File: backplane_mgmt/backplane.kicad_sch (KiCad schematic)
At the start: 16 parts, among them J201 Backplane, SW201 Blue, U201 74HC2G17, U202 74LVC1G07, U203 AT24CS32-SSHM

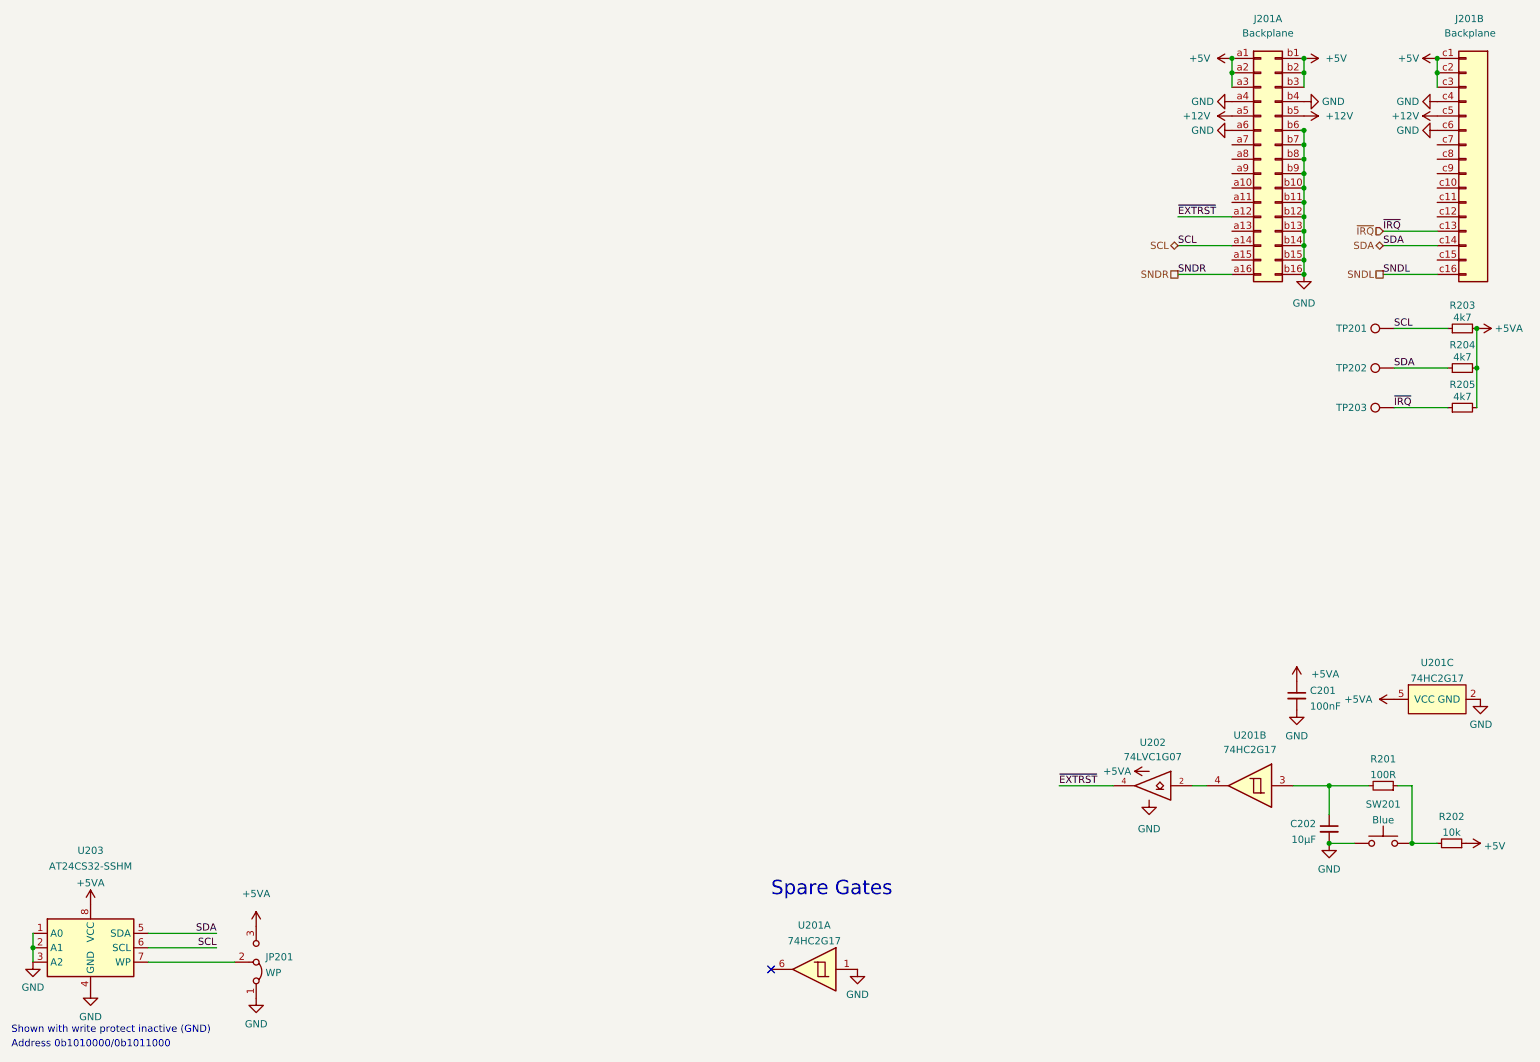
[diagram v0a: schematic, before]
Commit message: Routed backplane mgmt board
- Finished routing of the complete backplane management board; it
  doesn't do much other than provide power (with monitoring) and an
  audio output (with volume control) from the backplane.

  Originally this was gonna have a display but there's no space on the
  front panel for that.
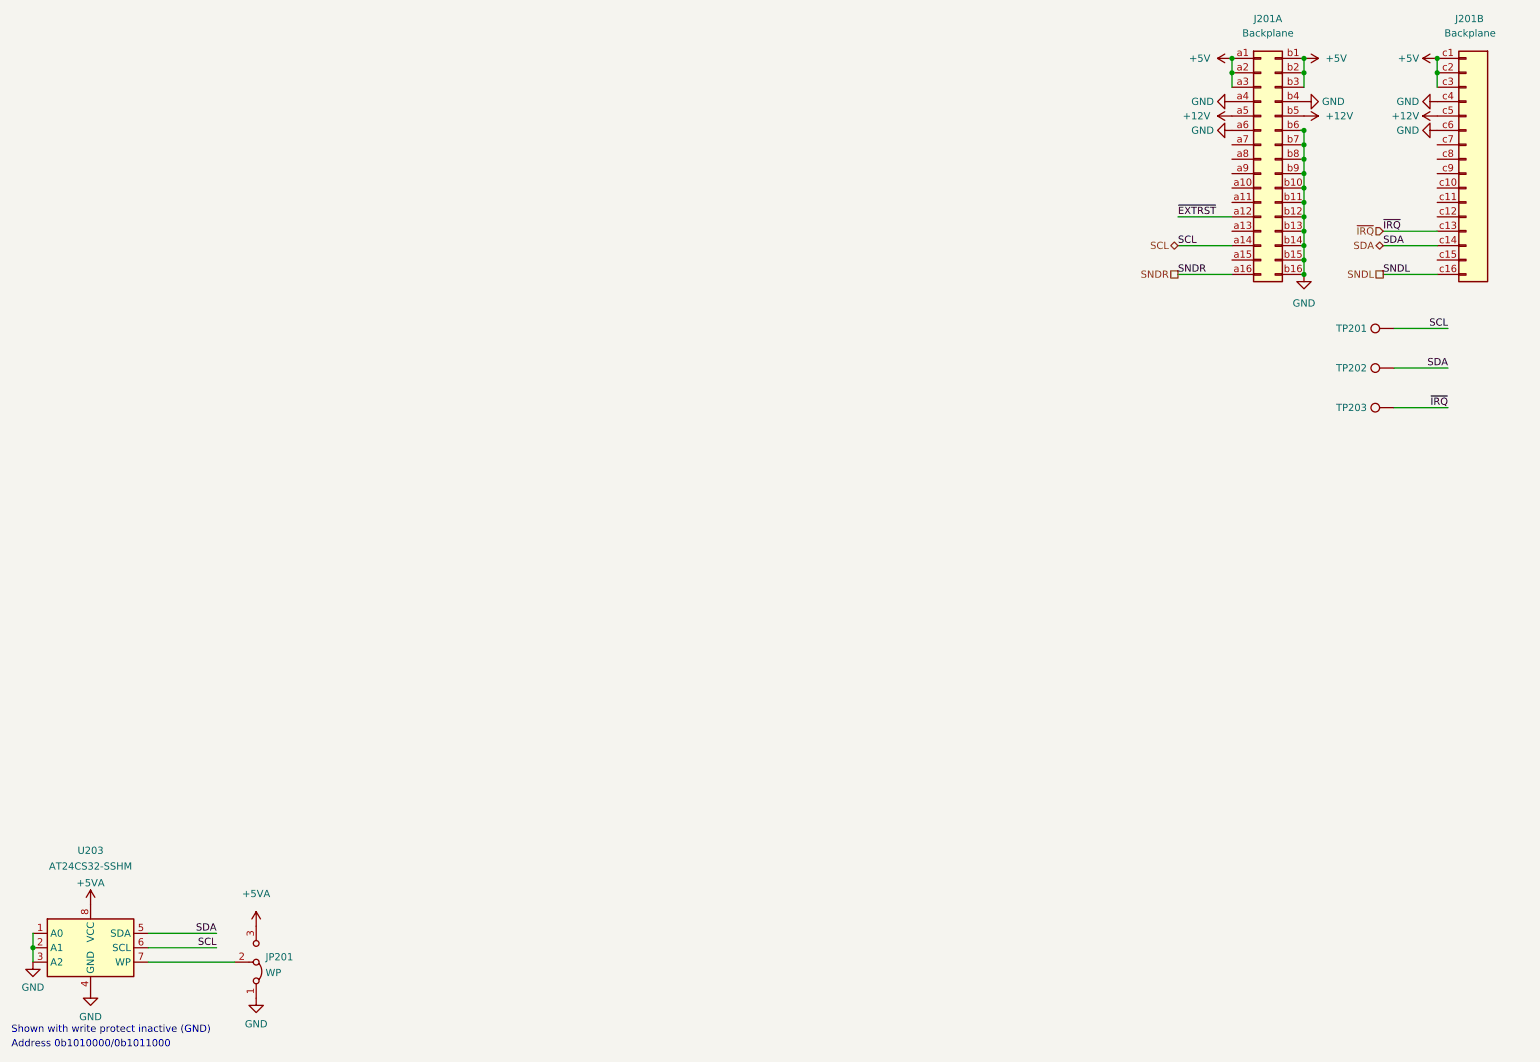
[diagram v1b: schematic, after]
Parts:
- removed C201: 100nF, Capacitor_SMD:C_0805_2012Metric, symbol Device:C_Small
- removed C202: 10µF, Capacitor_SMD:C_0805_2012Metric, symbol Device:C_Small
- removed R201: 100R, Resistor_SMD:R_0805_2012Metric, symbol Device:R_Small
- removed R202: 10k, Resistor_SMD:R_0805_2012Metric, symbol Device:R_Small
- removed R203, R204, R205: 4k7, Resistor_SMD:R_0805_2012Metric, symbol Device:R_Small
- removed SW201: Blue, Button_Switch_THT:SW_Tactile_SPST_Angled_PTS645Vx83-2LFS, symbol Switch:SW_Push
- removed U201: 74HC2G17, Package_SO:TSOP-6_1.65x3.05mm_P0.95mm, symbol 68komputer-common:74HC2G17
- removed U202: 74LVC1G07, 68komputer-common:SC-74-5_1.5x2.9mm_P0.95mm, symbol 74xGxx:74LVC1G07
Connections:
- no-connect marks 1 -> 0
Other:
- note removed: "Spare Gates"

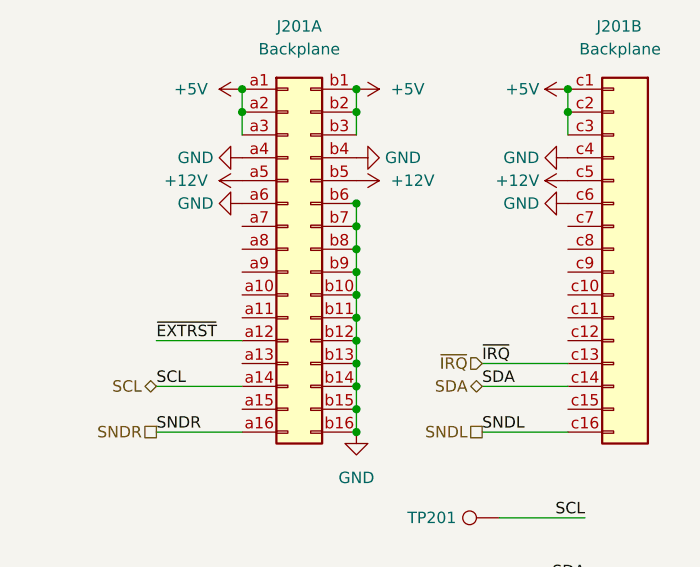
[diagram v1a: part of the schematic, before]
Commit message: Minor tweaks to all boards
- Moved around some traces on the 68000 CPU card for prettiness

- Added a connector on the backplane to provide +5V/+12V without a
  management card installed (for testing)
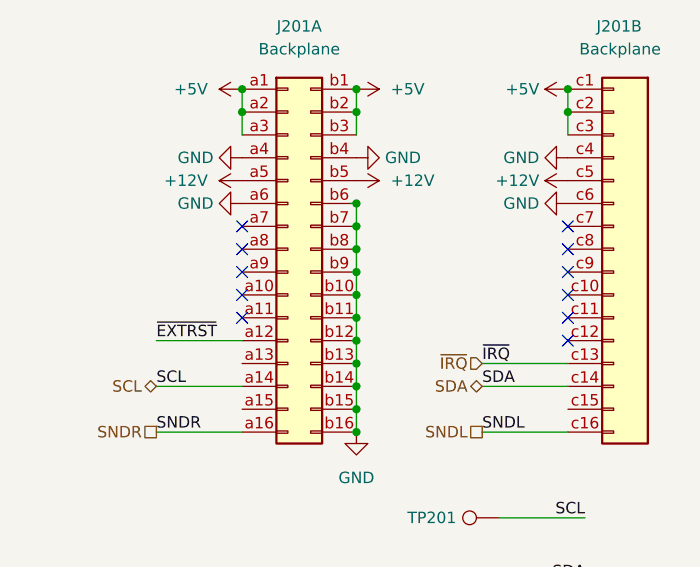
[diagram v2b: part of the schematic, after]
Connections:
- no-connect marks 0 -> 11
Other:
- company: (none) -> Tristan Seifert
- title: (none) -> Backplane Management and Power
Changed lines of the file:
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@@
 (kicad_sch (version 20211123) (generator eeschema)
   (paper "A4")
+  (title_block
+    (title "Backplane Management and Power")
+    (date "2022-01-09")
+    (rev "1")
+    (company "Tristan Seifert")
+  )
   (junction (at 245.11 24.13) (diameter 0) (color 0 0 0 0)
   )
@@
   (junction (at 20.955 178.435) (diameter 0) (color 0 0 0 0)
   )
+  (no_connect (at 232.41 46.99))
+  (no_connect (at 268.605 36.83))
+  (no_connect (at 232.41 44.45))
+  (no_connect (at 268.605 44.45))
+  (no_connect (at 268.605 41.91))
+  (no_connect (at 268.605 46.99))
+  (no_connect (at 232.41 41.91))
+  (no_connect (at 268.605 49.53))
+  (no_connect (at 232.41 39.37))
+  (no_connect (at 232.41 36.83))
+  (no_connect (at 268.605 39.37))
   (wire (pts (xy 245.11 59.69) (xy 245.11 57.15))
     (stroke (width 0) (type default) (color 0 0 0 0))

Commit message: Tweaks to bill of materials
- Added missing MPN's for a few components; tweaked a few bits of layout
  to increase some tolerances

  This includes kind of tweaking the boot rom socket positions in hopes
  of fitting fancier sockets
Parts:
- JP201: now left out of the parts list
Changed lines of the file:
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@@
   )
   (symbol (lib_id "Jumper:Jumper_3_Bridged12") (at 60.325 180.975 270) (mirror x) (unit 1)
-    (in_bom yes) (on_board yes) (fields_autoplaced)
+    (in_bom no) (on_board yes) (fields_autoplaced)
     (property "Reference" "JP201" (id 0) (at 61.976 180.0665 90)
       (effects (font (size 1.27 1.27)) (justify left))

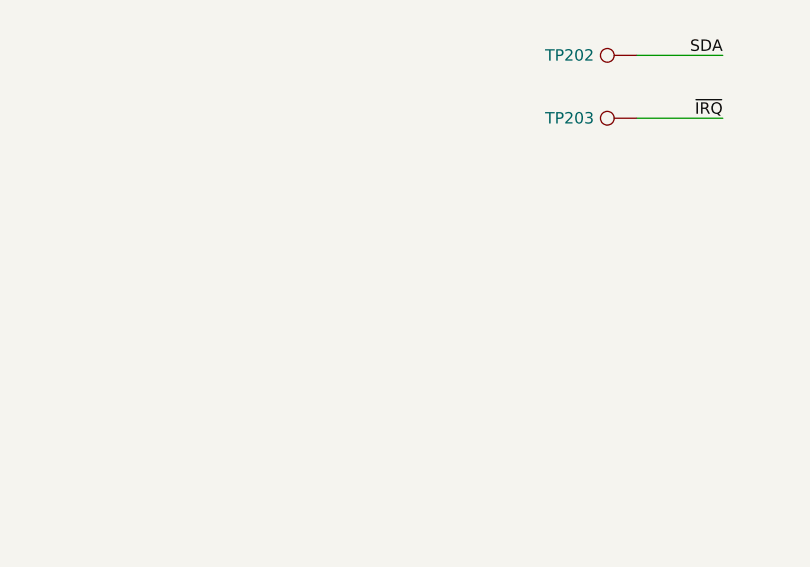
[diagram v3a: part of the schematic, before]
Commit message: Tweaks to backplane management board
- Added pull downs to the audio inputs, so that if the backplane doesn't
  provide audio, the op amp inputs aren't floating

- Minor tweaks to some of the routing. Also switched out the 5V
  regulator for a larger, easier to get version, and added some large
  planes for power dissapation.
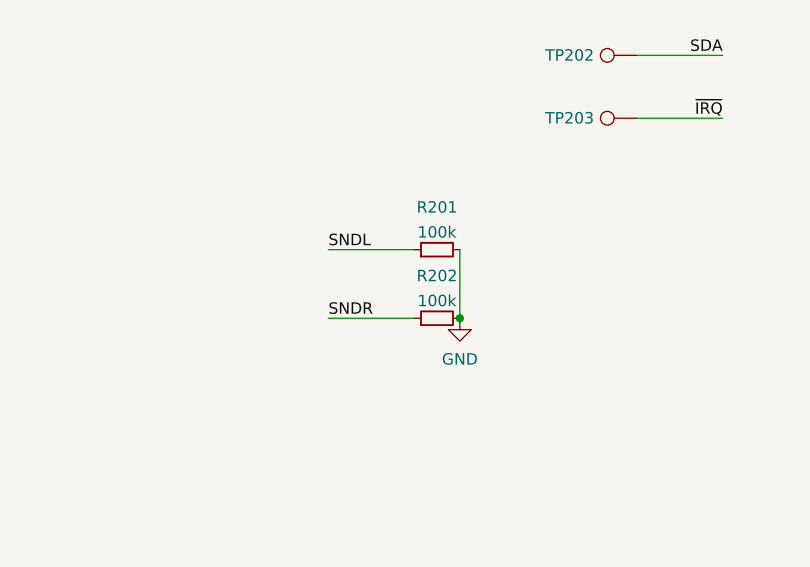
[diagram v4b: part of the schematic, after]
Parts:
- added R201, R202: 100k, Resistor_SMD:R_0805_2012Metric, symbol Device:R_Small
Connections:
- net GND: now also R201.2, R202.2
- net SNDL: now also R201.1
- net SNDR: now also R202.1
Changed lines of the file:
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@@
     (company "Tristan Seifert")
+  )
+  (junction (at 241.3 105.41) (diameter 0) (color 0 0 0 0)
   )
   (junction (at 245.11 24.13) (diameter 0) (color 0 0 0 0)
@@
     (stroke (width 0) (type default) (color 0 0 0 0))
   )
+  (wire (pts (xy 226.695 97.79) (xy 236.22 97.79))
+    (stroke (width 0) (type default) (color 0 0 0 0))
+  )
   (wire (pts (xy 41.275 180.975) (xy 56.515 180.975))
+    (stroke (width 0) (type default) (color 0 0 0 0))
+  )
+  (wire (pts (xy 226.695 105.41) (xy 236.22 105.41))
+    (stroke (width 0) (type default) (color 0 0 0 0))
+  )
+  (wire (pts (xy 241.3 97.79) (xy 241.3 105.41))
     (stroke (width 0) (type default) (color 0 0 0 0))
   )
@@
     (effects (font (size 1.27 1.27)) (justify left bottom))
   )
+  (label "SNDL" (at 226.695 97.79 0)
+    (effects (font (size 1.27 1.27)) (justify left bottom))
+  )
   (label "SDA" (at 270.51 76.2 180)
     (effects (font (size 1.27 1.27)) (justify right bottom))
   )
+  (label "SNDR" (at 226.695 105.41 0)
+    (effects (font (size 1.27 1.27)) (justify left bottom))
+  )
   (label "SNDR" (at 222.885 59.69 0)
     (effects (font (size 1.27 1.27)) (justify left bottom))
@@
     )
     (property "Datasheet" "" (id 3) (at 245.11 21.59 0)
+      (effects (font (size 1.27 1.27)) hide)
+    )
+    (pin "1")
+  )
+  (symbol (lib_id "power:GND") (at 241.3 105.41 0) (unit 1)
+    (in_bom yes) (on_board yes) (fields_autoplaced)
+    (property "Reference" "#PWR0110" (id 0) (at 241.3 111.76 0)
+      (effects (font (size 1.27 1.27)) hide)
+    )
+    (property "Value" "GND" (id 1) (at 241.3 109.9725 0))
+    (property "Footprint" "" (id 2) (at 241.3 105.41 0)
+      (effects (font (size 1.27 1.27)) hide)
+    )
+    (property "Datasheet" "" (id 3) (at 241.3 105.41 0)
       (effects (font (size 1.27 1.27)) hide)
     )
@@
     (pin "8")
   )
+  (symbol (lib_id "Device:R_Small") (at 238.76 105.41 90) (unit 1)
+    (in_bom yes) (on_board yes) (fields_autoplaced)
+    (property "Reference" "R202" (id 0) (at 238.76 100.7069 90))
+    (property "Value" "100k" (id 1) (at 238.76 103.482 90))
+    (property "Footprint" "Resistor_SMD:R_0805_2012Metric" (id 2) (at 238.76 105.41 0)
+      (effects (font (size 1.27 1.27)) hide)
+    )
+    (property "Datasheet" "~" (id 3) (at 238.76 105.41 0)
+      (effects (font (size 1.27 1.27)) hide)
+    )
+    (pin "1")
+    (pin "2")
+  )
   (symbol (lib_id "power:GND") (at 268.605 34.29 270) (unit 1)
     (in_bom yes) (on_board yes) (fields_autoplaced)
@@
     (pin "3")
   )
+  (symbol (lib_id "Device:R_Small") (at 238.76 97.79 90) (unit 1)
+    (in_bom yes) (on_board yes) (fields_autoplaced)
+    (property "Reference" "R201" (id 0) (at 238.76 93.0869 90))
+    (property "Value" "100k" (id 1) (at 238.76 95.862 90))
+    (property "Footprint" "Resistor_SMD:R_0805_2012Metric" (id 2) (at 238.76 97.79 0)
+      (effects (font (size 1.27 1.27)) hide)
+    )
+    (property "Datasheet" "~" (id 3) (at 238.76 97.79 0)
+      (effects (font (size 1.27 1.27)) hide)
+    )
+    (pin "1")
+    (pin "2")
+  )
   (symbol (lib_id "power:GND") (at 31.115 186.055 0) (unit 1)

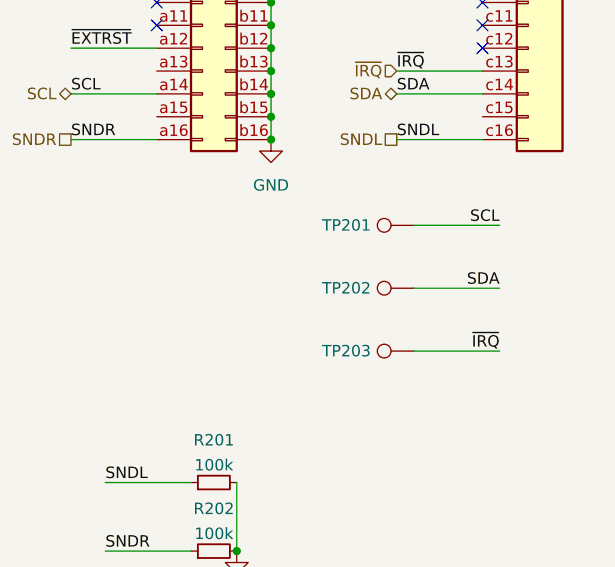
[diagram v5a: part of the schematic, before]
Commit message: Replaced current sense with shunt+INA209
- Instead of using unobtanium parts for the current sensing, we're
  instead just gonna use more of the shunt we already have to get for
  the current limit of the switching regulator, and then measuring the
  voltage drop with the INA209 which is functionally going to give us
  the same exact behavior as before.
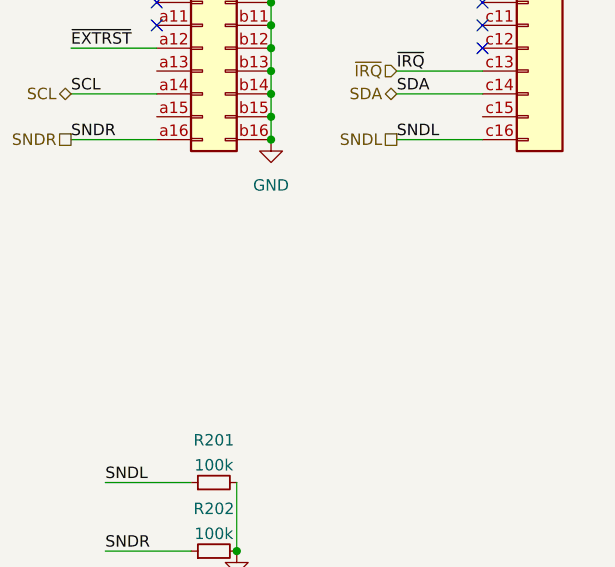
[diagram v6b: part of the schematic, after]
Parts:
- removed TP201: SCL, TestPoint:TestPoint_Loop_D2.60mm_Drill1.4mm_Beaded, symbol Connector:TestPoint
- removed TP202: SDA, TestPoint:TestPoint_Loop_D2.60mm_Drill1.4mm_Beaded, symbol Connector:TestPoint
- removed TP203: ~{IRQ}, TestPoint:TestPoint_Loop_D2.60mm_Drill1.4mm_Beaded, symbol Connector:TestPoint
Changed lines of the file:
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@@
-    (stroke (width 0) (type default) (color 0 0 0 0))
-  )
-  (wire (pts (xy 260.985 69.215) (xy 270.51 69.215))
     (stroke (width 0) (type default) (color 0 0 0 0))
   )
@@
     (stroke (width 0) (type default) (color 0 0 0 0))
   )
-  (wire (pts (xy 260.985 83.185) (xy 270.51 83.185))
-    (stroke (width 0) (type default) (color 0 0 0 0))
-  )
   (wire (pts (xy 245.11 49.53) (xy 245.11 46.99))
     (stroke (width 0) (type default) (color 0 0 0 0))
@@
     (stroke (width 0) (type default) (color 0 0 0 0))
   )
-  (wire (pts (xy 260.985 76.2) (xy 270.51 76.2))
-    (stroke (width 0) (type default) (color 0 0 0 0))
-  )
   (wire (pts (xy 245.11 44.45) (xy 245.11 41.91))
     (stroke (width 0) (type default) (color 0 0 0 0))
@@
     (effects (font (size 1.27 1.27)) (justify left bottom))
   )
-  (label "~{IRQ}" (at 270.51 83.185 180)
-    (effects (font (size 1.27 1.27)) (justify right bottom))
-  )
   (label "SNDL" (at 259.08 59.69 0)
     (effects (font (size 1.27 1.27)) (justify left bottom))
-  )
-  (label "SCL" (at 270.51 69.215 180)
-    (effects (font (size 1.27 1.27)) (justify right bottom))
   )
   (label "SCL" (at 53.34 178.435 180)
@@
   (label "SNDL" (at 226.695 97.79 0)
     (effects (font (size 1.27 1.27)) (justify left bottom))
-  )
-  (label "SDA" (at 270.51 76.2 180)
-    (effects (font (size 1.27 1.27)) (justify right bottom))
   )
   (label "SNDR" (at 226.695 105.41 0)
@@
     (pin "1")
   )
-  (symbol (lib_id "Connector:TestPoint") (at 260.985 69.215 90) (unit 1)
-    (in_bom yes) (on_board yes)
-    (property "Reference" "TP201" (id 0) (at 256.2098 69.215 90)
-      (effects (font (size 1.27 1.27)) (justify left))
-    )
-    (property "Value" "SCL" (id 1) (at 256.2098 68.072 90)
-      (effects (font (size 1.27 1.27)) (justify left) hide)
-    )
-    (property "Footprint" "TestPoint:TestPoint_Loop_D2.60mm_Drill1.4mm_Beaded" (id 2) (at 260.985 64.135 0)
-      (effects (font (size 1.27 1.27)) hide)
-    )
-    (property "Datasheet" "~" (id 3) (at 260.985 64.135 0)
-      (effects (font (size 1.27 1.27)) hide)
-    )
-    (property "MPN" "534-5001" (id 4) (at 260.985 69.215 90)
-      (effects (font (size 1.27 1.27)) hide)
-    )
-    (pin "1")
-  )
   (symbol (lib_id "Memory_EEPROM:AT24CS32-SSHM") (at 31.115 178.435 0) (unit 1)
     (in_bom yes) (on_board yes)
@@
     )
     (property "Datasheet" "" (id 3) (at 232.41 34.29 0)
-      (effects (font (size 1.27 1.27)) hide)
-    )
-    (pin "1")
-  )
-  (symbol (lib_id "Connector:TestPoint") (at 260.985 76.2 90) (unit 1)
-    (in_bom yes) (on_board yes)
-    (property "Reference" "TP202" (id 0) (at 256.2098 76.2 90)
-      (effects (font (size 1.27 1.27)) (justify left))
-    )
-    (property "Value" "SDA" (id 1) (at 256.2098 75.057 90)
-      (effects (font (size 1.27 1.27)) (justify left) hide)
-    )
-    (property "Footprint" "TestPoint:TestPoint_Loop_D2.60mm_Drill1.4mm_Beaded" (id 2) (at 260.985 71.12 0)
-      (effects (font (size 1.27 1.27)) hide)
-    )
-    (property "Datasheet" "~" (id 3) (at 260.985 71.12 0)
-      (effects (font (size 1.27 1.27)) hide)
-    )
-    (property "MPN" "534-5001" (id 4) (at 260.985 76.2 90)
       (effects (font (size 1.27 1.27)) hide)
     )
@@
     (pin "b9")
   )
-  (symbol (lib_id "Connector:TestPoint") (at 260.985 83.185 90) (unit 1)
-    (in_bom yes) (on_board yes)
-    (property "Reference" "TP203" (id 0) (at 256.2098 83.185 90)
-      (effects (font (size 1.27 1.27)) (justify left))
-    )
-    (property "Value" "~{IRQ}" (id 1) (at 256.2098 82.042 90)
-      (effects (font (size 1.27 1.27)) (justify left) hide)
-    )
-    (property "Footprint" "TestPoint:TestPoint_Loop_D2.60mm_Drill1.4mm_Beaded" (id 2) (at 260.985 78.105 0)
-      (effects (font (size 1.27 1.27)) hide)
-    )
-    (property "Datasheet" "~" (id 3) (at 260.985 78.105 0)
-      (effects (font (size 1.27 1.27)) hide)
-    )
-    (property "MPN" "534-5001" (id 4) (at 260.985 83.185 90)
-      (effects (font (size 1.27 1.27)) hide)
-    )
-    (pin "1")
-  )
 )
